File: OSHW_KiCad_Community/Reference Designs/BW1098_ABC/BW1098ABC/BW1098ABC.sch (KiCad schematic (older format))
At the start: 10 parts

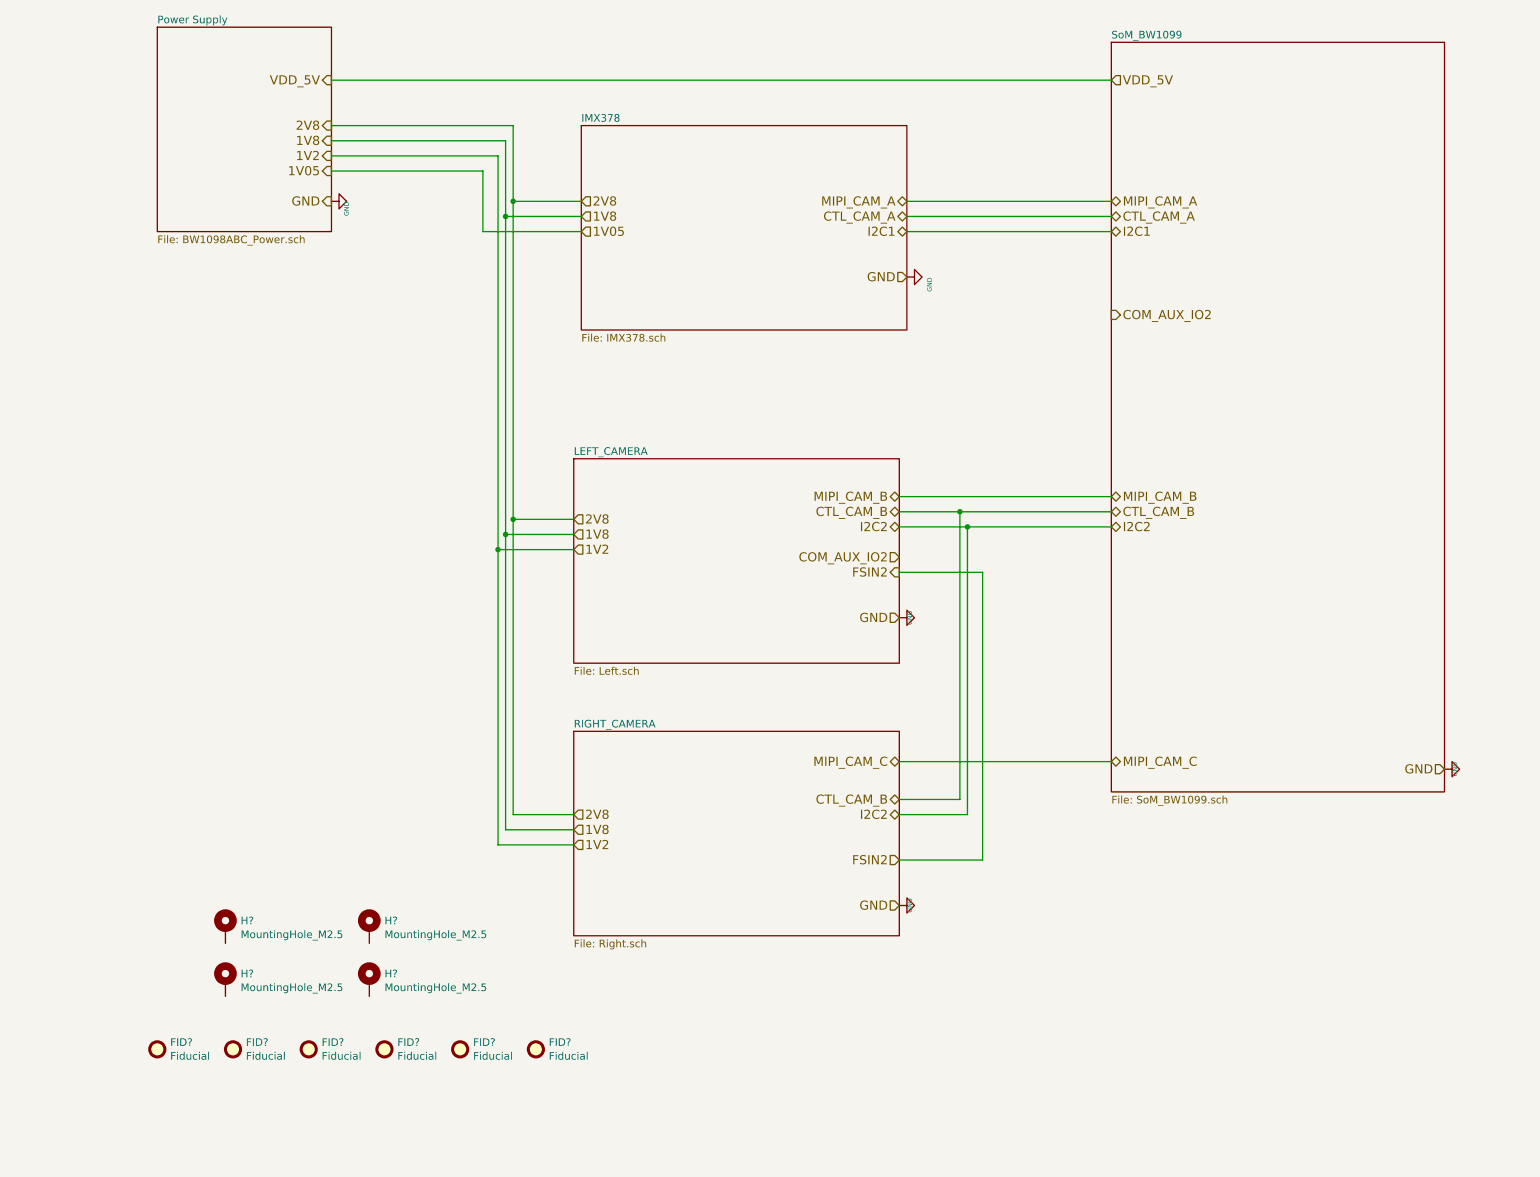
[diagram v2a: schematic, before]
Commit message: added busses, fixed hierarchical labeling, just need to fix an erc thing with my buses then itll pass
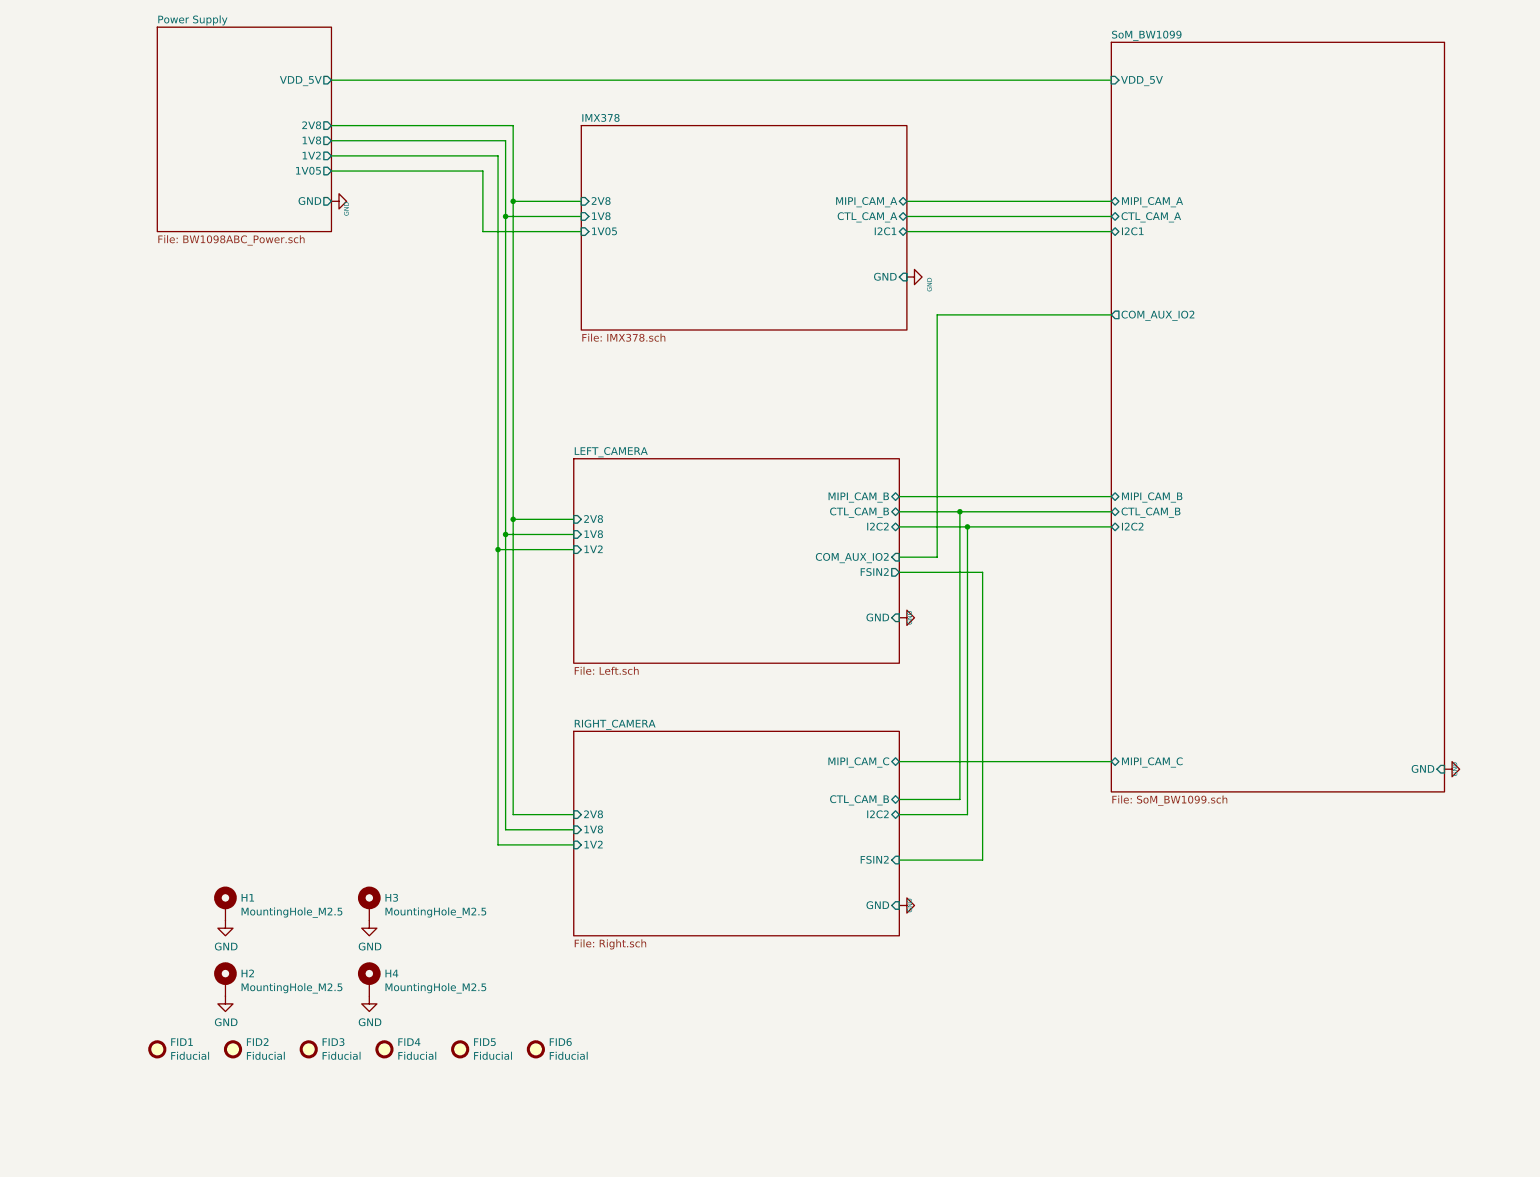
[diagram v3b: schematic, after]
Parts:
- gave numbers to parts that had none: 10
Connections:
- net GND: now also H1.1, H2.1, H3.1, H4.1
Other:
- moved on the sheet: H1, H3
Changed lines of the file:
@@
 F0 "SoM_BW1099" 50
 F1 "SoM_BW1099.sch" 50
-$EndSheet
-$Sheet
-S 4550 1400 2150 1350
-U 5FF8D4A5
-F0 "IMX378" 50
-F1 "IMX378.sch" 50
+F2 "MIPI_CAM_B" B L 8050 3850 50
+F3 "MIPI_CAM_C" B L 8050 5600 50
+F4 "I2C2" B L 8050 4050 50
+F5 "VDD_5V" I L 8050 1100 50
+F6 "GND" I R 10250 5650 50
+F7 "COM_AUX_IO2" O L 8050 2650 50
+F8 "CTL_CAM_A" B L 8050 2000 50
+F9 "I2C1" B L 8050 2100 50
+F10 "MIPI_CAM_A" B L 8050 1900 50
+F11 "CTL_CAM_B" B L 8050 3950 50
 $EndSheet
 $Sheet
@@
 F0 "RIGHT_CAMERA" 50
 F1 "Right.sch" 50
-$EndSheet
-$Sheet
-S 4500 3600 2150 1350
-U 5FF8D2B3
-F0 "LEFT_CAMERA" 50
-F1 "Left.sch" 50
-$EndSheet
-Text HLabel 8050 3850 2    60   BiDi ~ 0
-MIPI_CAM_B
-Text HLabel 8050 1900 2    60   BiDi ~ 0
-MIPI_CAM_A
-Text HLabel 8050 5600 2    60   BiDi ~ 0
-MIPI_CAM_C
-Text HLabel 8050 4050 2    60   BiDi ~ 0
-I2C2
-Text HLabel 8050 2100 2    60   BiDi ~ 0
-I2C1
-Text HLabel 8050 2000 2    60   BiDi ~ 0
-CTL_CAM_A
-Text HLabel 8050 3950 2    60   BiDi ~ 0
-CTL_CAM_B
-Text HLabel 8050 1100 2    60   Input ~ 0
-VDD_5V
-Text HLabel 10250 5650 0    60   Input ~ 0
-GND
-Text HLabel 8050 2650 2    60   Output ~ 0
-COM_AUX_IO2
-Text HLabel 4550 1900 2    60   Input ~ 0
-2V8
-Text HLabel 4550 2100 2    60   Input ~ 0
-1V05
-Text HLabel 6700 2100 0    60   BiDi ~ 0
-I2C1
-Text HLabel 6700 1900 0    60   BiDi ~ 0
-MIPI_CAM_A
-Text HLabel 6700 2000 0    60   BiDi ~ 0
-CTL_CAM_A
-Text HLabel 6700 2400 0    60   Input ~ 0
-GND
-Text HLabel 4550 2000 2    60   Input ~ 0
-1V8
-Text HLabel 6650 5600 0    60   BiDi ~ 0
-MIPI_CAM_C
-Text HLabel 6650 5950 0    60   BiDi ~ 0
-I2C2
-Text HLabel 4500 6150 2    60   Input ~ 0
-1V2
-Text HLabel 4500 5950 2    60   Input ~ 0
-2V8
-Text HLabel 6650 6550 0    60   Input ~ 0
-GND
-Text HLabel 4500 6050 2    60   Input ~ 0
-1V8
-Text HLabel 6650 6250 0    60   Input ~ 0
-FSIN2
-Text HLabel 6650 5850 0    60   BiDi ~ 0
-CTL_CAM_B
-Text HLabel 4500 4200 2    60   Input ~ 0
-1V2
-Text HLabel 4500 4000 2    60   Input ~ 0
-2V8
-Text HLabel 4500 4100 2    60   Input ~ 0
-1V8
+F2 "MIPI_CAM_C" B R 6650 5600 50
+F3 "2V8" I L 4500 5950 50
+F4 "1V8" I L 4500 6050 50
+F5 "1V2" I L 4500 6150 50
+F6 "FSIN2" I R 6650 6250 50
+F7 "I2C2" B R 6650 5950 50
+F8 "CTL_CAM_B" B R 6650 5850 50
+F9 "GND" I R 6650 6550 50
+$EndSheet
 $Comp
 L power:GND #GND_066
@@
 	0    -1   -1   0
 $EndComp
-Text HLabel 2900 1900 0    60   Output ~ 0
-GND
-Text HLabel 2900 1700 0    60   Output ~ 0
-1V05
-Text HLabel 2900 1500 0    60   Output ~ 0
-1V8
-Text HLabel 2900 1400 0    60   Output ~ 0
-2V8
-Text HLabel 2900 1600 0    60   Output ~ 0
-1V2
-Text HLabel 2900 1100 0    60   Output ~ 0
-VDD_5V
-$Comp
-L Mechanical:Fiducial FID?
+$Comp
+L Mechanical:Fiducial FID1
 U 1 1 6049A903
 P 1750 7500
-F 0 "FID?" H 1835 7546 50  0000 L CNN
+F 0 "FID1" H 1835 7546 50  0000 L CNN
 F 1 "Fiducial" H 1835 7455 50  0000 L CNN
 F 2 "Fiducial:Fiducial_1mm_Mask2mm" H 1750 7500 50  0001 C CNN
@@
 $EndComp
 $Comp
-L Mechanical:Fiducial FID?
+L Mechanical:Fiducial FID2
 U 1 1 5FF51DEB
 P 2250 7500
-F 0 "FID?" H 2335 7546 50  0000 L CNN
+F 0 "FID2" H 2335 7546 50  0000 L CNN
 F 1 "Fiducial" H 2335 7455 50  0000 L CNN
 F 2 "Fiducial:Fiducial_1mm_Mask2mm" H 2250 7500 50  0001 C CNN
@@
 $EndComp
 $Comp
-L Mechanical:Fiducial FID?
+L Mechanical:Fiducial FID3
 U 1 1 6049A905
 P 2750 7500
-F 0 "FID?" H 2835 7546 50  0000 L CNN
+F 0 "FID3" H 2835 7546 50  0000 L CNN
 F 1 "Fiducial" H 2835 7455 50  0000 L CNN
 F 2 "Fiducial:Fiducial_1mm_Mask2mm" H 2750 7500 50  0001 C CNN
@@
 $EndComp
 $Comp
-L Mechanical:Fiducial FID?
+L Mechanical:Fiducial FID4
 U 1 1 6049A906
 P 3250 7500
-F 0 "FID?" H 3335 7546 50  0000 L CNN
+F 0 "FID4" H 3335 7546 50  0000 L CNN
 F 1 "Fiducial" H 3335 7455 50  0000 L CNN
 F 2 "Fiducial:Fiducial_1mm_Mask2mm" H 3250 7500 50  0001 C CNN
@@
 $EndComp
 $Comp
-L Mechanical:Fiducial FID?
+L Mechanical:Fiducial FID5
 U 1 1 6049A907
 P 3750 7500
-F 0 "FID?" H 3835 7546 50  0000 L CNN
+F 0 "FID5" H 3835 7546 50  0000 L CNN
 F 1 "Fiducial" H 3835 7455 50  0000 L CNN
 F 2 "Fiducial:Fiducial_1mm_Mask2mm" H 3750 7500 50  0001 C CNN
@@
 $EndComp
 $Comp
-L Mechanical:Fiducial FID?
+L Mechanical:Fiducial FID6
 U 1 1 5FF52F7A
 P 4250 7500
-F 0 "FID?" H 4335 7546 50  0000 L CNN
+F 0 "FID6" H 4335 7546 50  0000 L CNN
 F 1 "Fiducial" H 4335 7455 50  0000 L CNN
 F 2 "Fiducial:Fiducial_1mm_Mask2mm" H 4250 7500 50  0001 C CNN
@@
 $EndComp
 $Comp
-L BW1098ABC-rescue:Mechanical_MountingHole_Pad-depthAI_sch H?
+L BW1098ABC-rescue:Mechanical_MountingHole_Pad-depthAI_sch H1
 U 1 1 5FF5350B
-P 2200 6700
-F 0 "H?" H 2300 6749 50  0000 L CNN
-F 1 "MountingHole_M2.5" H 2300 6658 50  0000 L CNN
-F 2 "fp_luxonis:Mounting_Wuerth_WA-SMSI-M2_H3mm_9774030243" H 2200 6700 50  0001 C CNN
-F 3 "" H 2200 6700 50  0001 C CNN
-	1    2200 6700
-	1    0    0    -1
-$EndComp
-$Comp
-L BW1098ABC-rescue:Mechanical_MountingHole_Pad-depthAI_sch H?
+P 2200 6550
+F 0 "H1" H 2300 6599 50  0000 L CNN
+F 1 "MountingHole_M2.5" H 2300 6508 50  0000 L CNN
+F 2 "fp_luxonis:Mounting_Wuerth_WA-SMSI-M2_H3mm_9774030243" H 2200 6550 50  0001 C CNN
+F 3 "" H 2200 6550 50  0001 C CNN
+	1    2200 6550
+	1    0    0    -1
+$EndComp
+$Comp
+L BW1098ABC-rescue:Mechanical_MountingHole_Pad-depthAI_sch H2
 U 1 1 5FF56FF7
 P 2200 7050
-F 0 "H?" H 2300 7099 50  0000 L CNN
+F 0 "H2" H 2300 7099 50  0000 L CNN
 F 1 "MountingHole_M2.5" H 2300 7008 50  0000 L CNN
 F 2 "fp_luxonis:Mounting_Wuerth_WA-SMSI-M2_H3mm_9774030243" H 2200 7050 50  0001 C CNN
@@
 $EndComp
 $Comp
-L BW1098ABC-rescue:Mechanical_MountingHole_Pad-depthAI_sch H?
+L BW1098ABC-rescue:Mechanical_MountingHole_Pad-depthAI_sch H4
 U 1 1 5FF572C3
 P 3150 7050
-F 0 "H?" H 3250 7099 50  0000 L CNN
+F 0 "H4" H 3250 7099 50  0000 L CNN
 F 1 "MountingHole_M2.5" H 3250 7008 50  0000 L CNN
 F 2 "fp_luxonis:Mounting_Wuerth_WA-SMSI-M2_H3mm_9774030243" H 3150 7050 50  0001 C CNN
@@
 $EndComp
 $Comp
-L BW1098ABC-rescue:Mechanical_MountingHole_Pad-depthAI_sch H?
+L BW1098ABC-rescue:Mechanical_MountingHole_Pad-depthAI_sch H3
 U 1 1 5FF57937
-P 3150 6700
-F 0 "H?" H 3250 6749 50  0000 L CNN
-F 1 "MountingHole_M2.5" H 3250 6658 50  0000 L CNN
-F 2 "fp_luxonis:Mounting_Wuerth_WA-SMSI-M2_H3mm_9774030243" H 3150 6700 50  0001 C CNN
-F 3 "" H 3150 6700 50  0001 C CNN
-	1    3150 6700
+P 3150 6550
+F 0 "H3" H 3250 6599 50  0000 L CNN
+F 1 "MountingHole_M2.5" H 3250 6508 50  0000 L CNN
+F 2 "fp_luxonis:Mounting_Wuerth_WA-SMSI-M2_H3mm_9774030243" H 3150 6550 50  0001 C CNN
+F 3 "" H 3150 6550 50  0001 C CNN
+	1    3150 6550
 	1    0    0    -1
 $EndComp
@@
 	0    -1   -1   0
 $EndComp
-Text HLabel 6650 4250 0    60   Input ~ 0
-COM_AUX_IO2
-Text HLabel 6650 4350 0    60   Output ~ 0
-FSIN2
-Text HLabel 6650 4650 0    60   Input ~ 0
-GND
-Text HLabel 6650 3850 0    60   BiDi ~ 0
-MIPI_CAM_B
-Text HLabel 6650 3950 0    60   BiDi ~ 0
-CTL_CAM_B
-Text HLabel 6650 4050 0    60   BiDi ~ 0
-I2C2
 Wire Wire Line
 	2900 1400 4100 1400
@@
 F0 "Power Supply" 50
 F1 "BW1098ABC_Power.sch" 50
+F2 "VDD_5V" O R 2900 1100 50
+F3 "1V2" O R 2900 1600 50
+F4 "1V8" O R 2900 1500 50
+F5 "2V8" O R 2900 1400 50
+F6 "1V05" O R 2900 1700 50
+F7 "GND" O R 2900 1900 50
 $EndSheet
 Wire Wire Line
@@
 Wire Wire Line
 	2900 1100 8050 1100
+$Sheet
+S 4550 1400 2150 1350
+U 5FF8D4A5
+F0 "IMX378" 50
+F1 "IMX378.sch" 50
+F2 "2V8" I L 4550 1900 50
+F3 "1V8" I L 4550 2000 50
+F4 "1V05" I L 4550 2100 50
+F5 "GND" I R 6700 2400 50
+F6 "CTL_CAM_A" B R 6700 2000 50
+F7 "I2C1" B R 6700 2100 50
+F8 "MIPI_CAM_A" B R 6700 1900 50
+$EndSheet
+Wire Wire Line
+	8050 2650 6900 2650
+Wire Wire Line
+	6900 2650 6900 4250
+Wire Wire Line
+	6900 4250 6650 4250
+$Sheet
+S 4500 3600 2150 1350
+U 5FF8D2B3
+F0 "LEFT_CAMERA" 50
+F1 "Left.sch" 50
+F2 "FSIN2" O R 6650 4350 50
+F3 "2V8" I L 4500 4000 50
+F4 "1V8" I L 4500 4100 50
+F5 "1V2" I L 4500 4200 50
+F6 "GND" I R 6650 4650 50
+F7 "COM_AUX_IO2" I R 6650 4250 50
+F8 "MIPI_CAM_B" B R 6650 3850 50
+F9 "CTL_CAM_B" B R 6650 3950 50
+F10 "I2C2" B R 6650 4050 50
+$EndSheet
+$Comp
+L power:GND #PWR0107
+U 1 1 6106C817
+P 2200 6650
+F 0 "#PWR0107" H 2200 6400 50  0001 C CNN
+F 1 "GND" H 2205 6477 50  0000 C CNN
+F 2 "" H 2200 6650 50  0001 C CNN
+F 3 "" H 2200 6650 50  0001 C CNN
+	1    2200 6650
+	1    0    0    -1
+$EndComp
+$Comp
+L power:GND #PWR0108
+U 1 1 6106D903
+P 3150 6650
+F 0 "#PWR0108" H 3150 6400 50  0001 C CNN
+F 1 "GND" H 3155 6477 50  0000 C CNN
+F 2 "" H 3150 6650 50  0001 C CNN
+F 3 "" H 3150 6650 50  0001 C CNN
+	1    3150 6650
+	1    0    0    -1
+$EndComp
+$Comp
+L power:GND #PWR0109
+U 1 1 6106E6FC
+P 3150 7150
+F 0 "#PWR0109" H 3150 6900 50  0001 C CNN
+F 1 "GND" H 3155 6977 50  0000 C CNN
+F 2 "" H 3150 7150 50  0001 C CNN
+F 3 "" H 3150 7150 50  0001 C CNN
+	1    3150 7150
+	1    0    0    -1
+$EndComp
+$Comp
+L power:GND #PWR0110
+U 1 1 6106EA7D
+P 2200 7150
+F 0 "#PWR0110" H 2200 6900 50  0001 C CNN
+F 1 "GND" H 2205 6977 50  0000 C CNN
+F 2 "" H 2200 7150 50  0001 C CNN
+F 3 "" H 2200 7150 50  0001 C CNN
+	1    2200 7150
+	1    0    0    -1
+$EndComp
 $EndSCHEMATC
